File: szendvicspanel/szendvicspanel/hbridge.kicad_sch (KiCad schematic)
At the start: 10 parts, among them Q1 BS170, Q2 BS170, Q3 BS170, Q4 BS170, Q5 BS250, Q6 BS250

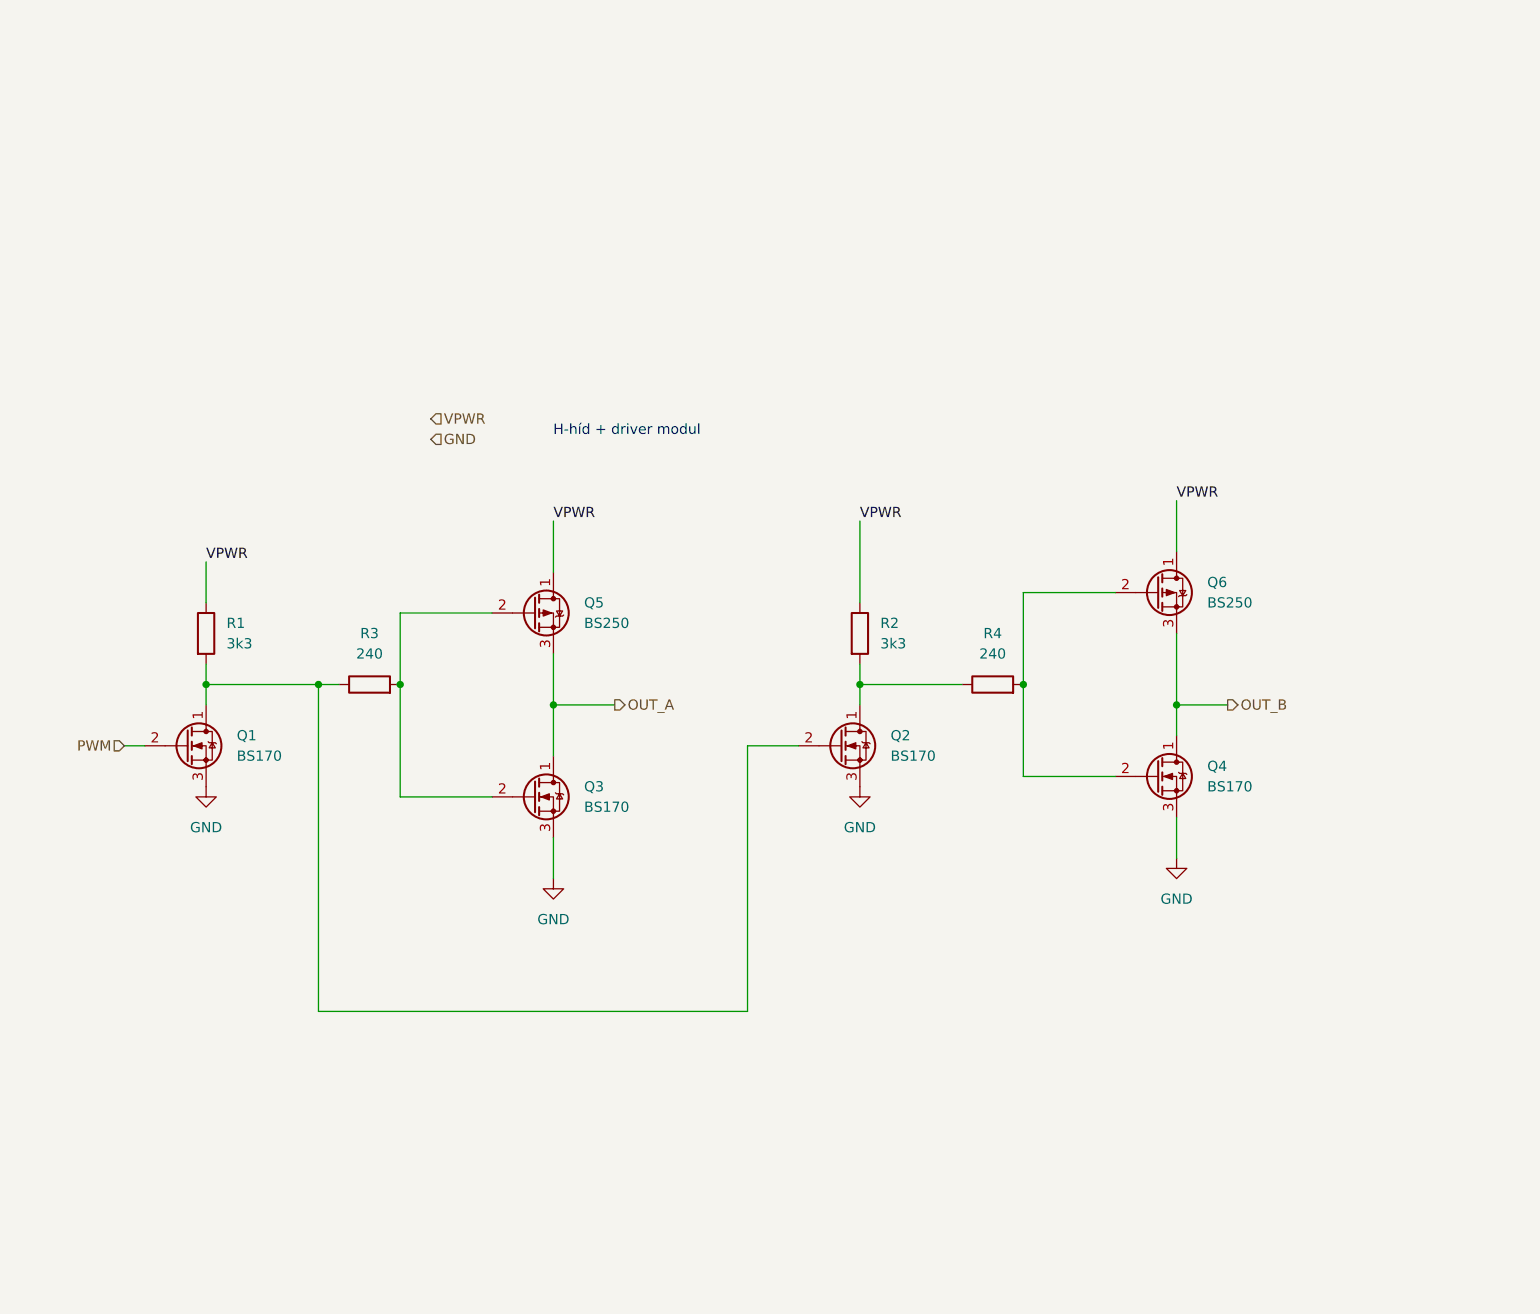
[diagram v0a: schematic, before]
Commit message: H-híd schematic módosítás
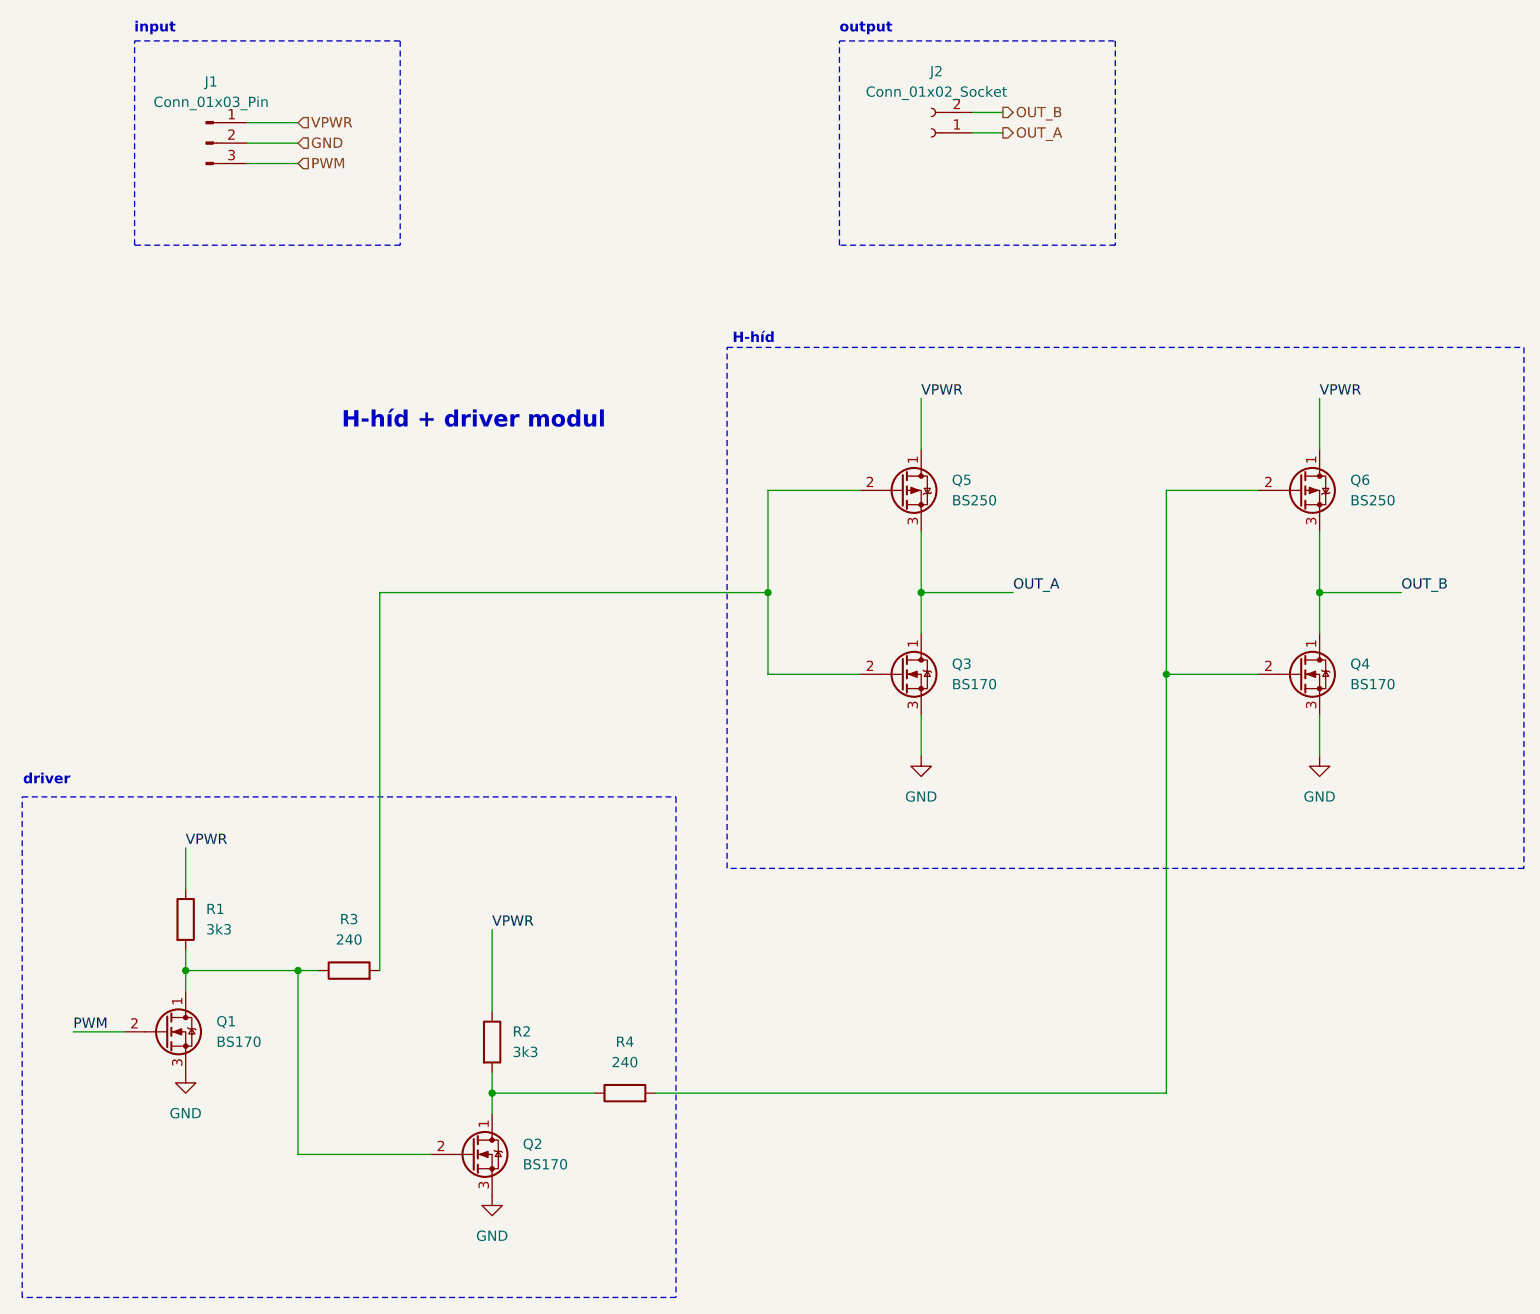
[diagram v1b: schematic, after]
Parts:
- added J1: Conn_01x03_Pin, symbol Connector:Conn_01x03_Pin
- added J2: Conn_01x02_Socket, symbol Connector:Conn_01x02_Socket
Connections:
- net GND: now also J1.2 (Pin_2)
- net OUT_A: now also J2.1 (Pin_1)
- net OUT_B: now also J2.2 (Pin_2)
- net PWM: now also J1.3 (Pin_3)
- net VPWR: now also J1.1 (Pin_1)
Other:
- note added: "H-híd"
- note added: "driver"
- note added: "input"
- note added: "output"
- company: (none) -> G.David
- title: (none) -> H-híd modul
- moved on the sheet: Q1, Q2, Q3, Q4, Q5, Q6, R1, R2, R3, R4
